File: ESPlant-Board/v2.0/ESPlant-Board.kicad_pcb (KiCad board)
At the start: 2 copper layers, 24 x 181.8 mm, 31 parts, among them J1 Conn_02x04_Counter_Clockwise, U1 ESP32-S2-MINI-1-N4, U2 BH-AAA-B5AK001, U3 Reset, U4 Boot, U5 Temp/Humid-Sensor, U6 Light sensor, U7 AMS1117-3_3, U8 MK-12C02-G025

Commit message: Board: Update panel
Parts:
- removed R5: 10k, Resistor_SMD:R_0402_1005Metric
- removed R7: 1M, Resistor_SMD:R_0402_1005Metric
- removed U2: BH-AAA-B5AK001, CustomFootprints:BAT-SMD_BH-AAA-B5AA001
- added U9: ~, CustomFootprints:AAA Battery-spring, B.Cu at (248.5, 149.1)
- C3: value 1uF -> 150pF
- J1: value Conn_02x04_Counter_Clockwise -> Conn_01x05; footprint Connector_PinHeader_2.54mm:PinHeader_2x04_P2.54mm_Vertical -> Connector_PinHeader_2.54mm:PinHeader_1x05_P2.54mm_Vertical
- moved C1 84.3 mm to (258.4, 140.8)
- moved C2 79.7 mm to (238.6, 141.0)
- moved C5 77.0 mm to (257.2, 117.7)
- moved U3 76.2 mm to (256.5, 136.0), turned to 90 degrees
- moved U4 75.9 mm to (240.5, 136.0), turned to -90 degrees
- moved C8 74.5 mm to (240.5, 116.5), turned to 90 degrees
- moved C7 73.7 mm to (254.9, 119.0), turned to 90 degrees
- moved C9 73.0 mm to (239.5, 116.5), turned to 90 degrees
- moved R4 72.7 mm to (241.1, 117.9)
- moved R6 71.4 mm to (243.1, 117.9), turned to 0 degrees
- moved BZ1 70.4 mm to (248.5, 142.5), turned to 180 degrees
- moved USB1 68.5 mm to (255.4, 125.6), turned to 90 degrees
- moved U6 67.8 mm to (257.1, 107.6)
- moved C3 66.9 mm to (257.8, 142.7), turned to 180 degrees
- moved D2 65.8 mm to (256.0, 144.4)
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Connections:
- J1 pad 1: /RX -> GND
- J1 pad 2: +3V3 -> /RX
- J1 pad 3: /IO0 -> /TX
- J1 pad 4: unconnected-(J1-Pin_4-Pad4) -> /IO0
- J1 pad 5: /IO2 -> +3V3
- R6 pad 2: /Voltage_Measurement_Select_2 -> /Voltage_Measurement_Select
- U1 pad 10: unconnected-(U1-IO6-Pad10) -> /Voltage_Measurement_Analog
- U1 pad 20: /LED_GREEN -> /Voltage_Measurement_Select
- U1 pad 21: /LED_RED -> /Square_Wave_Signal
- U1 pad 29: /Square_Wave_Signal -> unconnected-(U1-IO34-Pad29)
- U1 pad 32: /Light_Sensor_In -> /Light_Sensor_Select_1
- U1 pad 33: /Light_Sensor_Select_1 -> unconnected-(U1-IO37-Pad33)
- U1 pad 34: /Voltage_Measurement_Select_2 -> /TH_SDA
- U1 pad 35: /Voltage_Measurement_Select_1 -> /TH_SCL
- U1 pad 36: unconnected-(U1-IO40-Pad36) -> /Light_Sensor_In
- U1 pad 37: /TH_SDA -> /LED_RED
- U1 pad 38: /TH_SCL -> /LED_GREEN
- U1 pad 6: /IO2 -> unconnected-(U1-IO2-Pad6)
- U1 pad 7: /Voltage_Measurement_Analog -> /Light_Sensor_Analog
- U1 pad 8: /Light_Sensor_Analog -> unconnected-(U1-IO4-Pad8)
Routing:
- net /SensorCapV: track 95.6 -> 30.5 mm
- net /IO2: track 32.6 -> 0.00 mm, vias 1 -> 0
- net GND: track 37.3 -> 9.77 mm, vias 12 -> 17
- net /Voltage_Measurement_Select_2: track 25.5 -> 0.00 mm, vias 2 -> 0
- net /Voltage_Measurement_Select_1: track 25.3 -> 0.00 mm, vias 2 -> 0
- net +3V3: track 93.6 -> 70.4 mm, vias 6 -> 7
- net /EN: track 26.2 -> 47.9 mm, vias 4 -> 2
- net /TX: track 47.0 -> 25.4 mm, vias 1 -> 2
- net /Light_Sensor_Select_1: track 27.6 -> 7.01 mm, vias 2 -> 0
- net /Light_Sensor_In: track 20.7 -> 3.60 mm, vias 2 -> 0
- net /Buzzer: track 10.9 -> 25.9 mm, vias 0 -> 2
- net /Light_Sensor_Select_2: track 20.9 -> 7.37 mm, vias 2 -> 0
- net Net-(U9-+): track 9.59 -> 23.1 mm, vias 0 -> 2
- net /Light_Sensor_Analog: track 27.4 -> 39.5 mm
- net Net-(U2-+-Pad3): track 11.0 -> 0.00 mm
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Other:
- board size 24 x 181.8 mm -> 22 x 127 mm
- board text added: "+"
- board text added: "-"
- board text added: "30°"
- board text added: "M2"
- board text removed: "ES-Plant V2.0"
- board text removed: "IO2"
- board text removed: "JLCJLCJLCJLC"
- board text removed: "NC"

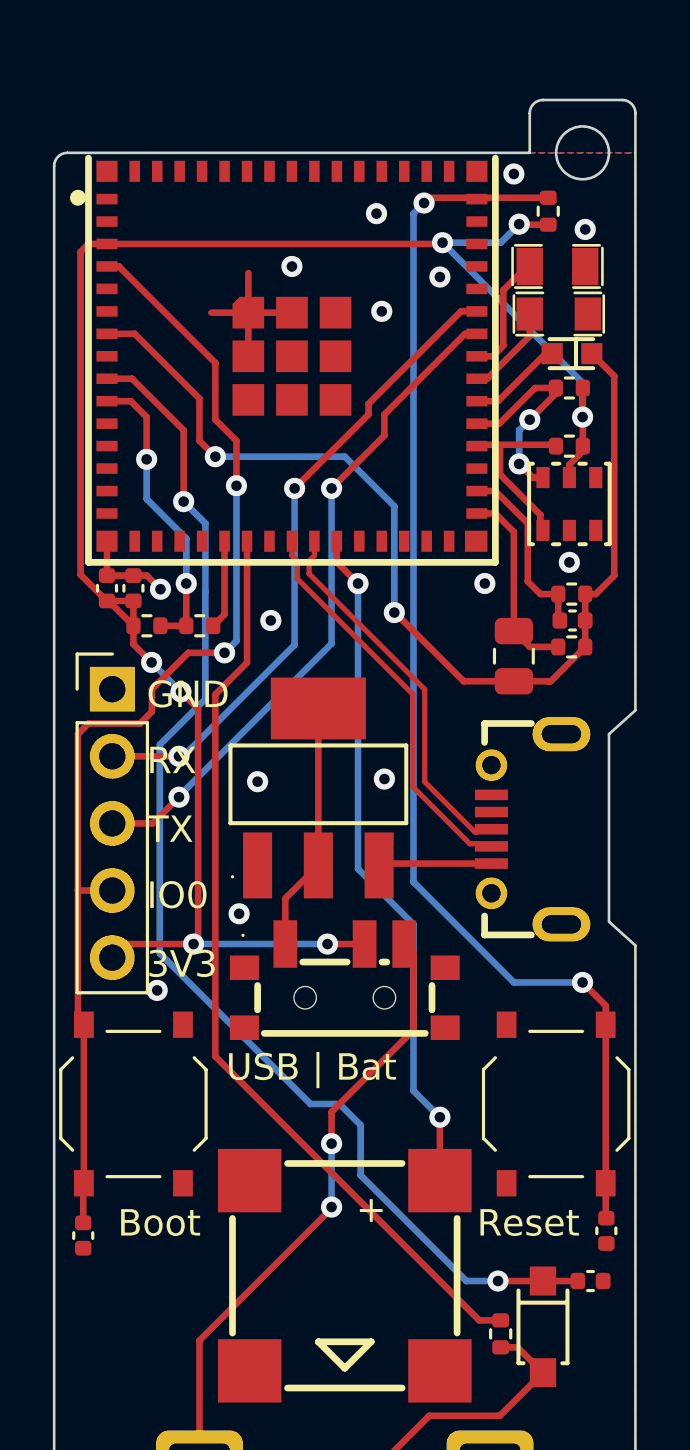
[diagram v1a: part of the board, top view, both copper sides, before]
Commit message: Board: Add panel for esp32-c6
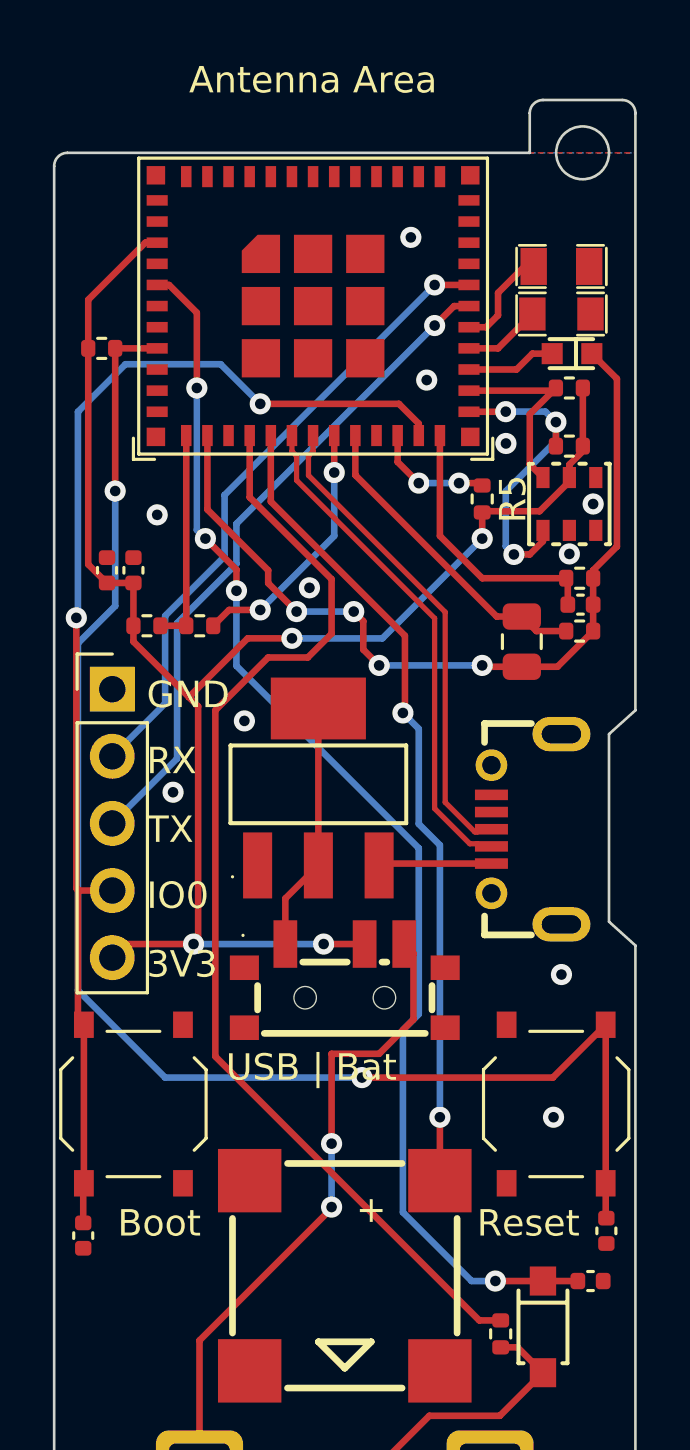
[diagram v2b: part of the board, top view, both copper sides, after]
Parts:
- added R5: 10k, Resistor_SMD:R_0402_1005Metric, F.Cu at (253.7, 113.1)
- U1: value ESP32-S2-MINI-1-N4 -> ESP32-C6-MINI-1/U; footprint CustomFootprints:WIFI-SMD_ESP32-MINI-1-N4 -> Espressif:ESP32-C6-MINI-1
- moved R9 17.7 mm to (239.3, 107.4), turned to 0 degrees
- moved U1 4.67 mm to (247.3, 103.1)
- moved C8 0.68 mm to (240.5, 115.8)
- moved C9 0.68 mm to (239.5, 115.8)
- moved R1 0.67 mm to (257.4, 116.1)
- moved R3 0.67 mm to (257.4, 118.1)
- moved C5 0.67 mm to (257.5, 117.1)
- moved C7 0.63 mm to (255.2, 118.5)
- moved D1 0.15 mm to (256.7, 104.3)
- moved D3 0.10 mm to (256.7, 106.1)
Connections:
- C2 pad 2: /IO0 -> /IO9
- J1 pad 2: /RX -> /TX
- J1 pad 3: /TX -> /RX
- J1 pad 4: /IO0 -> /IO9
- R9 pad 1: /EN -> +3V3
- R9 pad 2: +3V3 -> /EN
- U1 pad 10: /Voltage_Measurement_Analog -> unconnected-(U1-MTDI/GPIO5/ADC1_CH5-Pad10)
- U1 pad 11: unconnected-(U1-IO7-Pad11) -> GND
- U1 pad 12: unconnected-(U1-IO8-Pad12) -> /Voltage_Measurement_Analog
- U1 pad 13: unconnected-(U1-IO9-Pad13) -> /Light_Sensor_Analog
- U1 pad 14: unconnected-(U1-IO10-Pad14) -> GND
- U1 pad 15: unconnected-(U1-IO11-Pad15) -> /Square_Wave_Signal
- U1 pad 16: unconnected-(U1-IO12-Pad16) -> /Buzzer
- U1 pad 17: unconnected-(U1-IO13-Pad17) -> /D-
- U1 pad 18: unconnected-(U1-IO14-Pad18) -> /D+
- U1 pad 19: unconnected-(U1-IO15-Pad19) -> /Voltage_Measurement_Select
- U1 pad 20: /Voltage_Measurement_Select -> /Light_Sensor_Select_2
- U1 pad 21: /Square_Wave_Signal -> unconnected-(U1-NC-Pad21)
- U1 pad 22: unconnected-(U1-IO18-Pad22) -> /IO8
- U1 pad 23: /D- -> /IO9
- U1 pad 24: /D+ -> /Light_Sensor_Select_1
- U1 pad 25: /Buzzer -> /TH_SDA
- U1 pad 26: unconnected-(U1-IO26-Pad26) -> /TH_SCL
- U1 pad 27: unconnected-(U1-NC-Pad27) -> /Light_Sensor_In
- U1 pad 28: unconnected-(U1-IO33-Pad28) -> /LED_RED
- U1 pad 29: unconnected-(U1-IO34-Pad29) -> /LED_GREEN
- U1 pad 30: GND -> /RX
- U1 pad 31: /Light_Sensor_Select_2 -> /TX
- U1 pad 32: /Light_Sensor_Select_1 -> unconnected-(U1-NC-Pad32)
- U1 pad 34: /TH_SDA -> unconnected-(U1-NC-Pad34)
- U1 pad 35: /TH_SCL -> unconnected-(U1-NC-Pad35)
- U1 pad 36: /Light_Sensor_In -> GND
- U1 pad 37: /LED_RED -> GND
- U1 pad 38: /LED_GREEN -> GND
- U1 pad 39: /TX -> GND
- U1 pad 4: /IO0 -> unconnected-(U1-NC-Pad4)
- U1 pad 40: /RX -> GND
- U1 pad 41: unconnected-(U1-IO45-Pad41) -> GND
- U1 pad 44: unconnected-(U1-IO46-Pad44) -> GND
- U1 pad 45: /EN -> GND
- U1 pad 5: unconnected-(U1-IO1-Pad5) -> /AD_Capacitance
- U1 pad 7: /Light_Sensor_Analog -> unconnected-(U1-NC-Pad7)
- U1 pad 8: unconnected-(U1-IO4-Pad8) -> /EN
- U1 pad 9: /AD_Capacitance -> unconnected-(U1-MTMS/GPIO4/ADC1_CH4-Pad9)
- U4 pad 2: /IO0 -> /IO9
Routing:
- net /IO9: track 0.00 -> 47.2 mm, vias 0 -> 2
- net /IO0: track 44.3 -> 0.00 mm, vias 2 -> 0
- net GND: track 9.77 -> 0.04 mm, vias 17 -> 14
- net +3V3: track 70.4 -> 62.1 mm, vias 7 -> 4
- net /EN: track 47.9 -> 56.0 mm
- net /Square_Wave_Signal: track 34.9 -> 42.4 mm
- net /Light_Sensor_Analog: track 39.5 -> 32.6 mm, vias 2 -> 4
- net /Voltage_Measurement_Select: track 3.38 -> 9.79 mm, vias 0 -> 2
- net /TH_SDA: track 6.93 -> 12.0 mm, vias 0 -> 3
- net /Buzzer: track 25.9 -> 30.9 mm
- net /IO8: track 0.00 -> 4.57 mm, vias 0 -> 2
- net /Light_Sensor_Select_2: track 7.37 -> 11.9 mm
- net /D+: track 14.4 -> 18.4 mm
- net /D-: track 15.1 -> 19.1 mm
- net /Light_Sensor_Select_1: track 7.01 -> 10.3 mm
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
